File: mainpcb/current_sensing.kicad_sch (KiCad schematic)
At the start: 20 parts, among them J10 Conn_02x02_Top_Bottom, J11 Conn_02x02_Top_Bottom, U10 LM4040LP-4.1, U11 TMCS1108A3BQDR, U12 TMCS1108A3BQDR, U7 TMCS1108A3BQDR, U8 TMCS1108A3BQDR, U9 ADS7828

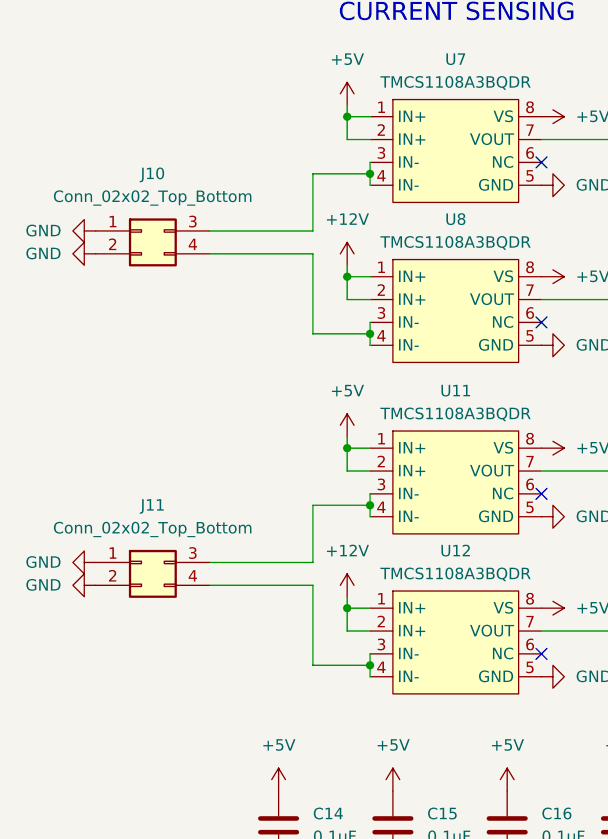
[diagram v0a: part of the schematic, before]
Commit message: Continued control board layout
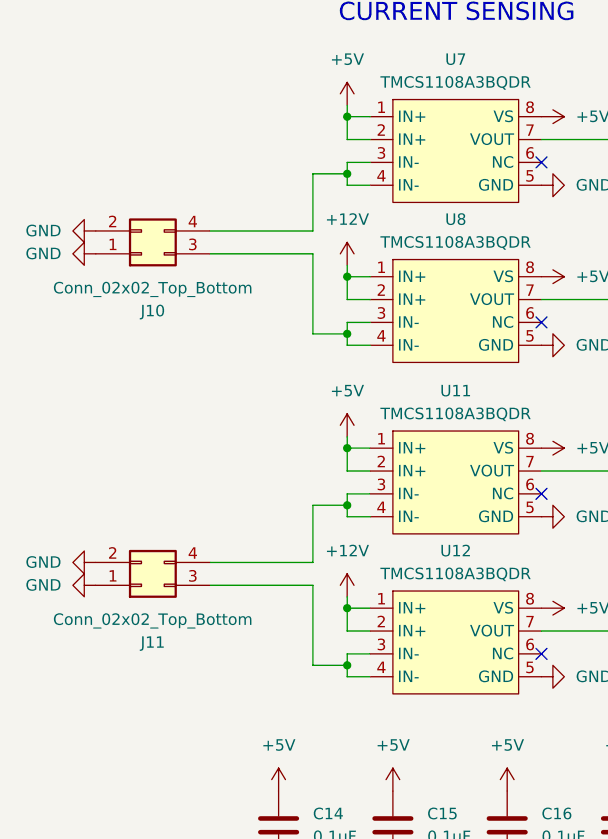
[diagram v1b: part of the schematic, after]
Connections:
- net at U12.3 (IN-), U12.4 (IN-): now also J11.3 (Pin_3); no longer J11.4 (Pin_4)
- net at U7.3 (IN-), U7.4 (IN-): now also J10.4 (Pin_4); no longer J10.3 (Pin_3)
- net at U8.3 (IN-), U8.4 (IN-): now also J10.3 (Pin_3); no longer J10.4 (Pin_4)
- net at U11.3 (IN-), U11.4 (IN-): now also J11.4 (Pin_4); no longer J11.3 (Pin_3)
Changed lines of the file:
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@@
 	)
 	(junction
-		(at 85.09 85.09)
+		(at 82.55 85.09)
 		(diameter 0)
 		(color 0 0 0 0)
@@
 	)
 	(junction
-		(at 85.09 121.92)
+		(at 82.55 121.92)
 		(diameter 0)
 		(color 0 0 0 0)
 	)
 	(junction
-		(at 85.09 104.14)
+		(at 82.55 104.14)
 		(diameter 0)
 		(color 0 0 0 0)
 	)
 	(junction
-		(at 85.09 67.31)
+		(at 82.55 67.31)
 		(diameter 0)
 		(color 0 0 0 0)
@@
 	(wire
 		(pts
-			(xy 78.74 121.92) (xy 85.09 121.92)
+			(xy 82.55 86.36) (xy 85.09 86.36)
+		)
+		(stroke
+			(width 0)
+			(type default)
+		)
+	)
+	(wire
+		(pts
+			(xy 78.74 121.92) (xy 82.55 121.92)
 		)
 		(stroke
@@
 	(wire
 		(pts
-			(xy 85.09 121.92) (xy 85.09 123.19)
+			(xy 82.55 121.92) (xy 82.55 123.19)
+		)
+		(stroke
+			(width 0)
+			(type default)
+		)
+	)
+	(wire
+		(pts
+			(xy 82.55 83.82) (xy 85.09 83.82)
 		)
 		(stroke
@@
 	(wire
 		(pts
+			(xy 67.31 110.49) (xy 78.74 110.49)
+		)
+		(stroke
+			(width 0)
+			(type default)
+		)
+	)
+	(wire
+		(pts
 			(xy 218.44 88.9) (xy 228.6 88.9)
 		)
@@
 	(wire
 		(pts
-			(xy 85.09 66.04) (xy 85.09 67.31)
+			(xy 82.55 66.04) (xy 82.55 67.31)
 		)
 		(stroke
@@
 	(wire
 		(pts
-			(xy 85.09 102.87) (xy 85.09 104.14)
+			(xy 82.55 102.87) (xy 82.55 104.14)
 		)
 		(stroke
@@
 	(wire
 		(pts
-			(xy 67.31 110.49) (xy 78.74 110.49)
+			(xy 67.31 73.66) (xy 78.74 73.66)
 		)
 		(stroke
@@
 	(wire
 		(pts
-			(xy 78.74 85.09) (xy 85.09 85.09)
+			(xy 82.55 120.65) (xy 85.09 120.65)
+		)
+		(stroke
+			(width 0)
+			(type default)
+		)
+	)
+	(wire
+		(pts
+			(xy 78.74 85.09) (xy 82.55 85.09)
 		)
 		(stroke
@@
 	(wire
 		(pts
-			(xy 78.74 104.14) (xy 85.09 104.14)
+			(xy 78.74 104.14) (xy 82.55 104.14)
 		)
 		(stroke
@@
 	(wire
 		(pts
+			(xy 82.55 105.41) (xy 85.09 105.41)
+		)
+		(stroke
+			(width 0)
+			(type default)
+		)
+	)
+	(wire
+		(pts
 			(xy 153.67 109.22) (xy 176.53 109.22)
 		)
@@
 	(wire
 		(pts
-			(xy 85.09 67.31) (xy 85.09 68.58)
+			(xy 82.55 67.31) (xy 82.55 68.58)
 		)
 		(stroke
@@
 	(wire
 		(pts
+			(xy 82.55 102.87) (xy 85.09 102.87)
+		)
+		(stroke
+			(width 0)
+			(type default)
+		)
+	)
+	(wire
+		(pts
 			(xy 173.99 106.68) (xy 143.51 106.68)
 		)
@@
 	(wire
 		(pts
-			(xy 78.74 67.31) (xy 85.09 67.31)
+			(xy 82.55 66.04) (xy 85.09 66.04)
+		)
+		(stroke
+			(width 0)
+			(type default)
+		)
+	)
+	(wire
+		(pts
+			(xy 78.74 67.31) (xy 82.55 67.31)
 		)
 		(stroke
@@
 	(wire
 		(pts
-			(xy 85.09 104.14) (xy 85.09 105.41)
+			(xy 82.55 104.14) (xy 82.55 105.41)
 		)
 		(stroke
@@
 	(wire
 		(pts
+			(xy 198.12 91.44) (xy 176.53 91.44)
+		)
+		(stroke
+			(width 0)
+			(type default)
+		)
+	)
+	(wire
+		(pts
 			(xy 67.31 113.03) (xy 78.74 113.03)
 		)
@@
 	(wire
 		(pts
-			(xy 198.12 91.44) (xy 176.53 91.44)
+			(xy 82.55 123.19) (xy 85.09 123.19)
 		)
 		(stroke
@@
 	(wire
 		(pts
-			(xy 85.09 83.82) (xy 85.09 85.09)
+			(xy 82.55 83.82) (xy 82.55 85.09)
 		)
 		(stroke
@@
 	(wire
 		(pts
-			(xy 85.09 120.65) (xy 85.09 121.92)
+			(xy 82.55 68.58) (xy 85.09 68.58)
 		)
 		(stroke
@@
 	(wire
 		(pts
-			(xy 78.74 113.03) (xy 78.74 121.92)
+			(xy 82.55 120.65) (xy 82.55 121.92)
 		)
 		(stroke
@@
 	(wire
 		(pts
-			(xy 116.84 86.36) (xy 198.12 86.36)
+			(xy 78.74 113.03) (xy 78.74 121.92)
 		)
 		(stroke
@@
 	(wire
 		(pts
-			(xy 67.31 73.66) (xy 78.74 73.66)
+			(xy 116.84 86.36) (xy 198.12 86.36)
 		)
 		(stroke
@@
 	(wire
 		(pts
-			(xy 85.09 85.09) (xy 85.09 86.36)
+			(xy 82.55 85.09) (xy 82.55 86.36)
 		)
 		(stroke
@@
 	(symbol
 		(lib_id "Connector_Generic:Conn_02x02_Top_Bottom")
-		(at 59.69 73.66 0)
+		(at 59.69 76.2 0)
+		(mirror x)
 		(unit 1)
 		(exclude_from_sim no)
@@
 		(on_board yes)
 		(dnp no)
-		(fields_autoplaced yes)
 		(property "Reference" "J10"
-			(at 60.96 67.31 0)
+			(at 60.96 82.55 0)
 			(effects
 				(font
@@
 		)
 		(property "Value" "Conn_02x02_Top_Bottom"
-			(at 60.96 69.85 0)
+			(at 60.96 80.01 0)
 			(effects
 				(font
@@
 		)
 		(property "Footprint" "Connector_Molex:Molex_Mini-Fit_Jr_5569-04A2_2x02_P4.20mm_Horizontal"
-			(at 59.69 73.66 0)
+			(at 59.69 76.2 0)
 			(effects
 				(font
@@
 		)
 		(property "Datasheet" "~"
-			(at 59.69 73.66 0)
+			(at 59.69 76.2 0)
 			(effects
 				(font
@@
 		)
 		(property "Description" "Generic connector, double row, 02x02, top/bottom pin numbering scheme (row 1: 1...pins_per_row, row2: pins_per_row+1 ... num_pins), script generated (kicad-library-utils/schlib/autogen/connector/)"
-			(at 59.69 73.66 0)
+			(at 59.69 76.2 0)
 			(effects
 				(font
@@
 		)
 		(property "Digikey" "https://www.digikey.ca/en/products/detail/molex/0039300040/930321"
-			(at 59.69 73.66 0)
+			(at 59.69 76.2 0)
 			(effects
 				(font
@@
 	(symbol
 		(lib_id "Connector_Generic:Conn_02x02_Top_Bottom")
-		(at 59.69 110.49 0)
+		(at 59.69 113.03 0)
+		(mirror x)
 		(unit 1)
 		(exclude_from_sim no)
@@
 		(on_board yes)
 		(dnp no)
-		(fields_autoplaced yes)
 		(property "Reference" "J11"
-			(at 60.96 104.14 0)
+			(at 60.96 119.38 0)
 			(effects
 				(font
@@
 		)
 		(property "Value" "Conn_02x02_Top_Bottom"
-			(at 60.96 106.68 0)
+			(at 60.96 116.84 0)
 			(effects
 				(font
@@
 		)
 		(property "Footprint" "Connector_Molex:Molex_Mini-Fit_Jr_5569-04A2_2x02_P4.20mm_Horizontal"
-			(at 59.69 110.49 0)
+			(at 59.69 113.03 0)
 			(effects
 				(font
@@
 		)
 		(property "Datasheet" "~"
-			(at 59.69 110.49 0)
+			(at 59.69 113.03 0)
 			(effects
 				(font
@@
 		)
 		(property "Description" "Generic connector, double row, 02x02, top/bottom pin numbering scheme (row 1: 1...pins_per_row, row2: pins_per_row+1 ... num_pins), script generated (kicad-library-utils/schlib/autogen/connector/)"
-			(at 59.69 110.49 0)
+			(at 59.69 113.03 0)
 			(effects
 				(font
@@
 		)
 		(property "Digikey" "https://www.digikey.ca/en/products/detail/molex/0039300040/930321"
-			(at 59.69 110.49 0)
+			(at 59.69 113.03 0)
 			(effects
 				(font

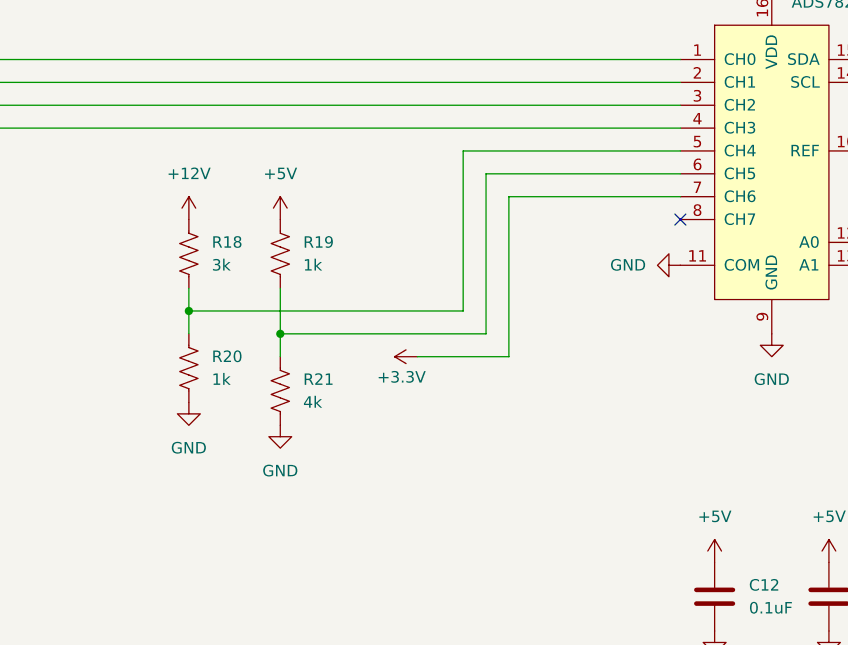
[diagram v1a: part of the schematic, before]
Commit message: Started signal track layout of control PCB
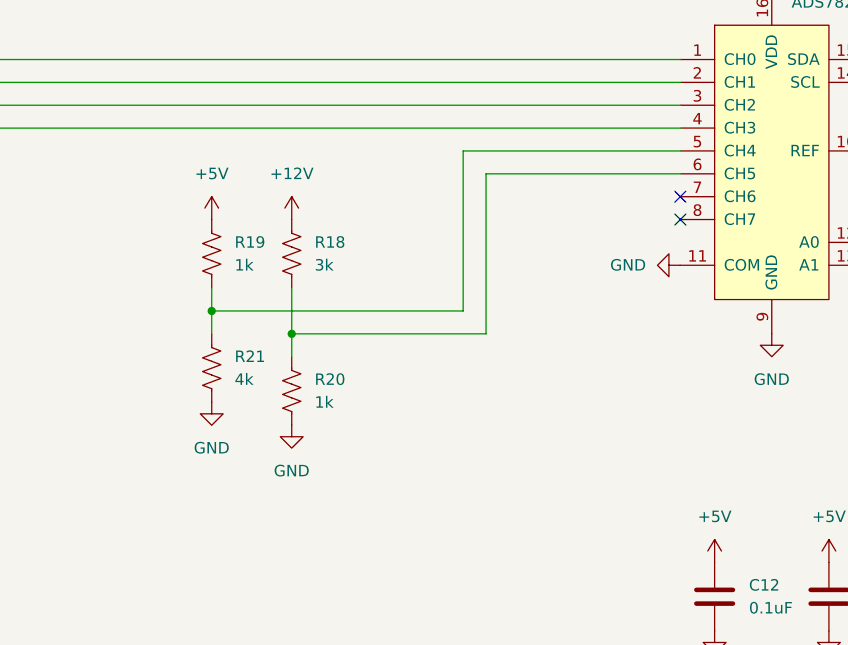
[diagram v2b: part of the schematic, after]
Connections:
- net at R19.2, R21.1: now also U9.5 (CH4); no longer U9.6 (CH5)
- net at R18.2, R20.1: now also U9.6 (CH5); no longer U9.5 (CH4)
- net +3.3V: no longer names the net of U9.7 (CH6)
- no-connect marks 5 -> 6
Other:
- moved on the sheet: R18, R19, R20, R21

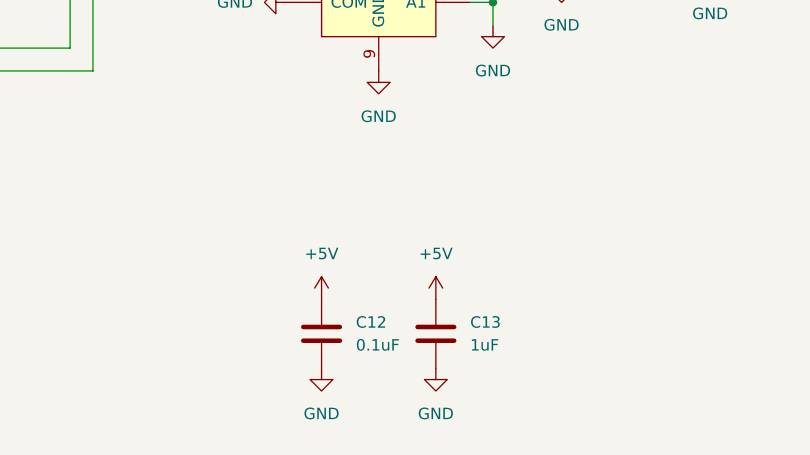
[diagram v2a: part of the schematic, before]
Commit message: Completed control board layout
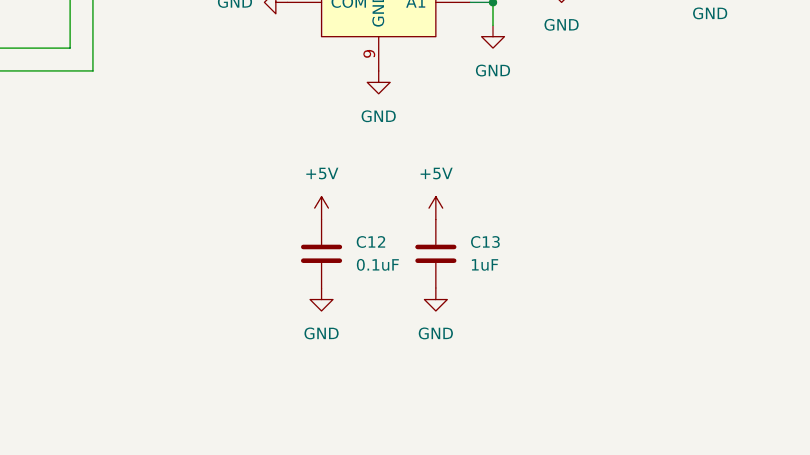
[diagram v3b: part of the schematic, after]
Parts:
- U11, U12, U7, U8: footprint Package_SO:SOIC-8-N7_3.9x4.9mm_P1.27mm -> Package_SO:SOIC-8_3.9x4.9mm_P1.27mm
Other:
- moved on the sheet: C12, C13
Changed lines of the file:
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@@
 			)
 		)
-		(property "Footprint" "Package_SO:SOIC-8-N7_3.9x4.9mm_P1.27mm"
+		(property "Footprint" "Package_SO:SOIC-8_3.9x4.9mm_P1.27mm"
 			(at 95.25 113.03 0)
 			(effects
@@
 	(symbol
 		(lib_id "power:GND")
-		(at 214.63 142.24 0)
+		(at 214.63 133.35 0)
 		(unit 1)
 		(exclude_from_sim no)
@@
 		(fields_autoplaced yes)
 		(property "Reference" "#PWR096"
-			(at 214.63 148.59 0)
+			(at 214.63 139.7 0)
 			(effects
 				(font
@@
 		)
 		(property "Value" "GND"
-			(at 214.63 147.32 0)
+			(at 214.63 138.43 0)
 			(effects
 				(font
@@
 		)
 		(property "Footprint" ""
-			(at 214.63 142.24 0)
+			(at 214.63 133.35 0)
 			(effects
 				(font
@@
 		)
 		(property "Datasheet" ""
-			(at 214.63 142.24 0)
+			(at 214.63 133.35 0)
 			(effects
 				(font
@@
 		)
 		(property "Description" "Power symbol creates a global label with name \"GND\" , ground"
-			(at 214.63 142.24 0)
+			(at 214.63 133.35 0)
 			(effects
 				(font
@@
 	(symbol
 		(lib_id "Device:C")
-		(at 214.63 138.43 0)
+		(at 214.63 129.54 0)
 		(unit 1)
 		(exclude_from_sim no)
@@
 		(fields_autoplaced yes)
 		(property "Reference" "C13"
-			(at 218.44 137.1599 0)
+			(at 218.44 128.2699 0)
 			(effects
 				(font
@@
 		)
 		(property "Value" "1uF"
-			(at 218.44 139.6999 0)
+			(at 218.44 130.8099 0)
 			(effects
 				(font
@@
 		)
 		(property "Footprint" "Capacitor_THT:C_Rect_L4.6mm_W2.0mm_P2.50mm_MKS02_FKP02"
-			(at 215.5952 142.24 0)
+			(at 215.5952 133.35 0)
 			(effects
 				(font
@@
 		)
 		(property "Datasheet" "~"
-			(at 214.63 138.43 0)
+			(at 214.63 129.54 0)
 			(effects
 				(font
@@
 		)
 		(property "Description" "Unpolarized capacitor"
-			(at 214.63 138.43 0)
+			(at 214.63 129.54 0)
 			(effects
 				(font
@@
 		)
 		(property "Digikey" "https://www.digikey.ca/en/products/detail/vishay-beyschlag-draloric-bc-components/K104K10X7RF5UH5/2356754"
-			(at 214.63 138.43 0)
+			(at 214.63 129.54 0)
 			(effects
 				(font
@@
 	(symbol
 		(lib_id "power:+5V")
-		(at 201.93 134.62 0)
+		(at 201.93 125.73 0)
 		(unit 1)
 		(exclude_from_sim no)
@@
 		(fields_autoplaced yes)
 		(property "Reference" "#PWR089"
-			(at 201.93 138.43 0)
+			(at 201.93 129.54 0)
 			(effects
 				(font
@@
 		)
 		(property "Value" "+5V"
-			(at 201.93 129.54 0)
+			(at 201.93 120.65 0)
 			(effects
 				(font
@@
 		)
 		(property "Footprint" ""
-			(at 201.93 134.62 0)
+			(at 201.93 125.73 0)
 			(effects
 				(font
@@
 		)
 		(property "Datasheet" ""
-			(at 201.93 134.62 0)
+			(at 201.93 125.73 0)
 			(effects
 				(font
@@
 		)
 		(property "Description" "Power symbol creates a global label with name \"+5V\""
-			(at 201.93 134.62 0)
+			(at 201.93 125.73 0)
 			(effects
 				(font
@@
 		(on_board yes)
 		(dnp no)
-		(fields_autoplaced yes)
 		(property "Reference" "C16"
 			(at 104.14 138.4299 0)
@@
 	(symbol
 		(lib_id "Device:C")
-		(at 201.93 138.43 0)
+		(at 201.93 129.54 0)
 		(unit 1)
 		(exclude_from_sim no)
@@
 		(fields_autoplaced yes)
 		(property "Reference" "C12"
-			(at 205.74 137.1599 0)
+			(at 205.74 128.2699 0)
 			(effects
 				(font
@@
 		)
 		(property "Value" "0.1uF"
-			(at 205.74 139.6999 0)
+			(at 205.74 130.8099 0)
 			(effects
 				(font
@@
 		)
 		(property "Footprint" "Capacitor_THT:C_Rect_L4.6mm_W2.0mm_P2.50mm_MKS02_FKP02"
-			(at 202.8952 142.24 0)
+			(at 202.8952 133.35 0)
 			(effects
 				(font
@@
 		)
 		(property "Datasheet" "~"
-			(at 201.93 138.43 0)
+			(at 201.93 129.54 0)
 			(effects
 				(font
@@
 		)
 		(property "Description" "Unpolarized capacitor"
-			(at 201.93 138.43 0)
+			(at 201.93 129.54 0)
 			(effects
 				(font
@@
 		)
 		(property "Digikey" "https://www.digikey.ca/en/products/detail/vishay-beyschlag-draloric-bc-components/K104K10X7RF5UH5/2356754"
-			(at 201.93 138.43 0)
+			(at 201.93 129.54 0)
 			(effects
 				(font
@@
 			)
 		)
-		(property "Footprint" "Package_SO:SOIC-8-N7_3.9x4.9mm_P1.27mm"
+		(property "Footprint" "Package_SO:SOIC-8_3.9x4.9mm_P1.27mm"
 			(at 95.25 76.2 0)
 			(effects
@@
 	(symbol
 		(lib_id "power:GND")
-		(at 201.93 142.24 0)
+		(at 201.93 133.35 0)
 		(unit 1)
 		(exclude_from_sim no)
@@
 		(fields_autoplaced yes)
 		(property "Reference" "#PWR095"
-			(at 201.93 148.59 0)
+			(at 201.93 139.7 0)
 			(effects
 				(font
@@
 		)
 		(property "Value" "GND"
-			(at 201.93 147.32 0)
+			(at 201.93 138.43 0)
 			(effects
 				(font
@@
 		)
 		(property "Footprint" ""
-			(at 201.93 142.24 0)
+			(at 201.93 133.35 0)
 			(effects
 				(font
@@
 		)
 		(property "Datasheet" ""
-			(at 201.93 142.24 0)
+			(at 201.93 133.35 0)
 			(effects
 				(font
@@
 		)
 		(property "Description" "Power symbol creates a global label with name \"GND\" , ground"
-			(at 201.93 142.24 0)
+			(at 201.93 133.35 0)
 			(effects
 				(font
@@
 			)
 		)
-		(property "Footprint" "Package_SO:SOIC-8-N7_3.9x4.9mm_P1.27mm"
+		(property "Footprint" "Package_SO:SOIC-8_3.9x4.9mm_P1.27mm"
 			(at 95.25 58.42 0)
 			(effects
@@
 			)
 		)
-		(property "Footprint" "Package_SO:SOIC-8-N7_3.9x4.9mm_P1.27mm"
+		(property "Footprint" "Package_SO:SOIC-8_3.9x4.9mm_P1.27mm"
 			(at 95.25 95.25 0)
 			(effects
@@
 	(symbol
 		(lib_id "power:+5V")
-		(at 214.63 134.62 0)
+		(at 214.63 125.73 0)
 		(unit 1)
 		(exclude_from_sim no)
@@
 		(fields_autoplaced yes)
 		(property "Reference" "#PWR090"
-			(at 214.63 138.43 0)
+			(at 214.63 129.54 0)
 			(effects
 				(font
@@
 		)
 		(property "Value" "+5V"
-			(at 214.63 129.54 0)
+			(at 214.63 120.65 0)
 			(effects
 				(font
@@
 		)
 		(property "Footprint" ""
-			(at 214.63 134.62 0)
+			(at 214.63 125.73 0)
 			(effects
 				(font
@@
 		)
 		(property "Datasheet" ""
-			(at 214.63 134.62 0)
+			(at 214.63 125.73 0)
 			(effects
 				(font
@@
 		)
 		(property "Description" "Power symbol creates a global label with name \"+5V\""
-			(at 214.63 134.62 0)
+			(at 214.63 125.73 0)
 			(effects
 				(font

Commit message: As-Produced commit
This commit contains the PCBs as they were sent to the manufacturer
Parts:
- U11, U12, U7: Digikey (none) -> https://www.digikey.ca/en/products/detail/texas-instruments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
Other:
- note added: "NOTE: TMCS1108A3UQDR USED IN MANUFACTURED MODEL. ONLY DIFFERENCE IS 0-AMP BIAS VOLTAGE. SEE DATASHEET"
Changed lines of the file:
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@@
 		)
 	)
+	(text "NOTE: TMCS1108A3UQDR USED IN MANUFACTURED\nMODEL. ONLY DIFFERENCE IS 0-AMP BIAS VOLTAGE.\nSEE DATASHEET"
+		(exclude_from_sim no)
+		(at 96.774 156.464 0)
+		(effects
+			(font
+				(size 1.27 1.27)
+			)
+		)
+	)
 	(global_label "SDA"
 		(shape input)
@@
 			)
 		)
+		(property "Digikey" "https://www.digikey.ca/en/products/detail/texas-instruments/TMCS1108A3UQDR/13692795"
+			(at 95.25 113.03 0)
+			(effects
+				(font
+					(size 1.27 1.27)
+				)
+				(hide yes)
+			)
+		)
 		(pin "4"
 		)
@@
 			)
 		)
+		(property "Digikey" "https://www.digikey.ca/en/products/detail/texas-instruments/TMCS1108A3UQDR/13692795"
+			(at 95.25 58.42 0)
+			(effects
+				(font
+					(size 1.27 1.27)
+				)
+				(hide yes)
+			)
+		)
 		(pin "4"
 		)
@@
 			(at 95.25 95.25 0)
 			(effects
+				(font
+					(size 1.27 1.27)
+				)
+				(hide yes)
+			)
+		)
+		(property "Digikey" "https://www.digikey.ca/en/products/detail/texas-instruments/TMCS1108A3UQDR/13692795"
+			(at 95.25 95.25 0)
+			(effects

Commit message: Added drawing information boxes
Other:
- note added: "AS-BUILT"
- note added: "BOT-HOVEN Control PCB Version 1"
- note added: "Drawn: Jascha Petersen"
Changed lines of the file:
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@@
+		)
+	)
+	(text "AS-BUILT"
+		(exclude_from_sim no)
+		(at 184.912 172.974 0)
+		(effects
+			(font
+				(size 2 2)
+				(italic yes)
+			)
+		)
+	)
+	(text "Drawn: Jascha Petersen"
+		(exclude_from_sim no)
+		(at 195.58 180.086 0)
+		(effects
+			(font
+				(size 2 2)
+			)
+		)
+	)
+	(text "BOT-HOVEN Control PCB Version 1"
+		(exclude_from_sim no)
+		(at 217.678 169.164 0)
+		(effects
+			(font
+				(size 3 3)
+				(thickness 0.6)
+				(bold yes)
+			)
 		)
 	)

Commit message: Added PDF schematic exports
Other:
- title: (none) -> Control PCB Current Sensing
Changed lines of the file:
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@@
 	(generator_version "8.0")
 	(paper "A4")
+	(title_block
+		(title "Control PCB Current Sensing")
+	)
 	(junction
 		(at 82.55 85.09)
